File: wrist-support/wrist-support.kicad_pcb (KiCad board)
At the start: 2 copper layers, 90.5 x 59 mm, 4 parts

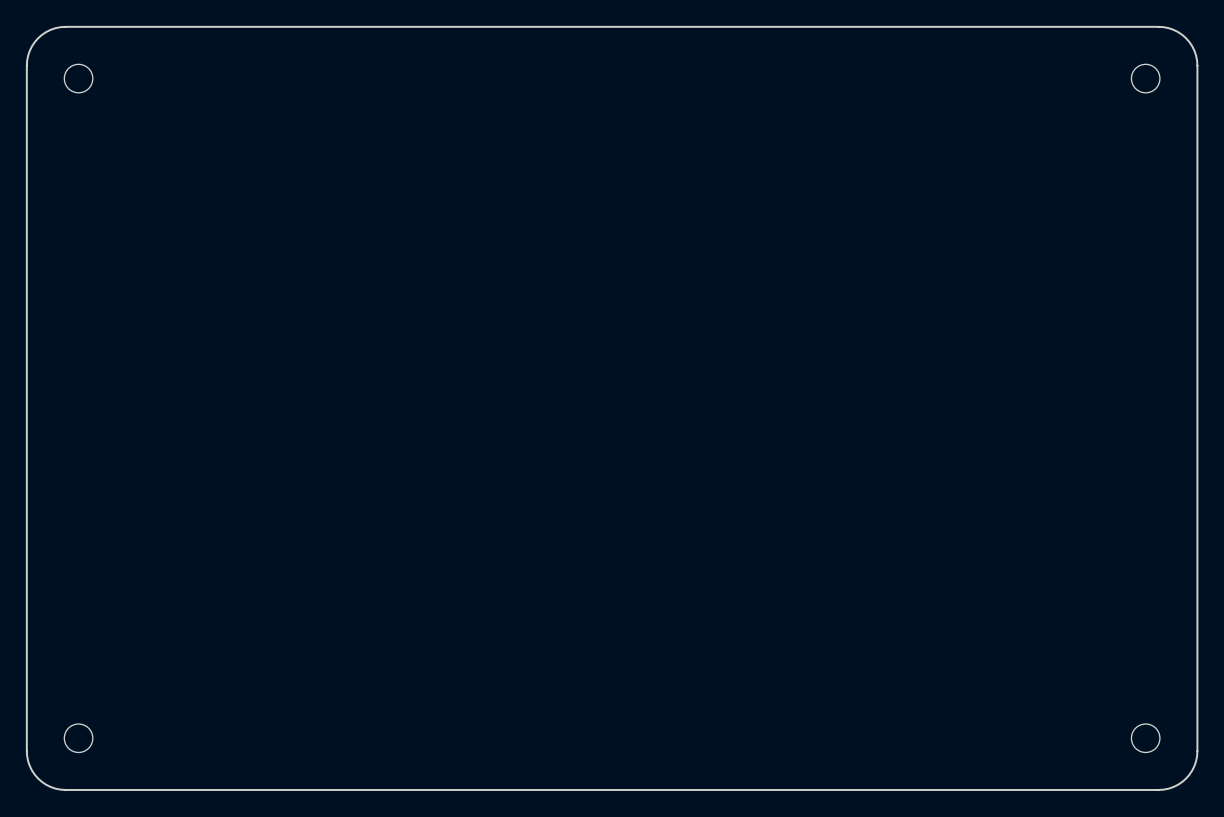
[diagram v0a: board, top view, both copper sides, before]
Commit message: Add gerbers and assembly files
M  .gitignore
M  MyFootprints.pretty/MountingHole_2.2mm_M2_ISO7380_Pad.kicad_mod
M  MySymbols.kicad_sym
M  README.md
M  drawborder.py
A  jlcpcb/gerber/optical-keyboard-mx-B_Cu.gbl
A  jlcpcb/gerber/optical-keyboard-mx-B_Mask.gbs
A  jlcpcb/gerber/optical-keyboard-mx-B_Paste.gbp
A  jlcpcb/gerber/optical-keyboard-mx-B_Silkscreen.gbo
A  jlcpcb/gerber/optical-keyboard-mx-Edge_Cuts.gm1
A  jlcpcb/gerber/optical-keyboard-mx-F_Cu.gtl
A  jlcpcb/gerber/optical-keyboard-mx-F_Mask.gts
A  jlcpcb/gerber/optical-keyboard-mx-F_Paste.gtp
A  jlcpcb/gerber/optical-keyboard-mx-F_Silkscreen.gto
A  jlcpcb/gerber/optical-keyboard-mx-NPTH-drl_map.gbr
A  jlcpcb/gerber/optical-keyboard-mx-NPTH.drl
A  jlcpcb/gerber/optical-keyboard-mx-PTH-drl_map.gbr
A  jlcpcb/gerber/optical-keyboard-mx-PTH.drl
M  led_driver.kicad_sch
M  mounting-hw.kicad_sch
M  optical-keyboard-mx.kicad_pcb
M  optical-keyboard-mx.kicad_sch
M  placefp.py
M  switch-plate/.gitignore
A  switch-plate/jlcpcb/gerber/switch-plate-B_Cu.gbl
A  switch-plate/jlcpcb/gerber/switch-plate-B_Mask.gbs
A  switch-plate/jlcpcb/gerber/switch-plate-B_Paste.gbp
A  switch-plate/jlcpcb/gerber/switch-plate-B_Silkscreen.gbo
A  switch-plate/jlcpcb/gerber/switch-plate-Edge_Cuts.gm1
A  switch-plate/jlcpcb/gerber/switch-plate-F_Cu.gtl
A  switch-plate/jlcpcb/gerber/switch-plate-F_Mask.gts
A  switch-plate/jlcpcb/gerber/switch-plate-F_Paste.gtp
A  switch-plate/jlcpcb/gerber/switch-plate-F_Silkscreen.gto
A  switch-plate/jlcpcb/gerber/switch-plate-NPTH-drl_map.gbr
A  switch-plate/jlcpcb/gerber/switch-plate-NPTH.drl
A  switch-plate/jlcpcb/gerber/switch-plate-PTH-drl_map.gbr
A  switch-plate/jlcpcb/gerber/switch-plate-PTH.drl
M  switch-plate/switch-plate.kicad_pcb
M  switch-plate/switch-plate.kicad_prl
M  switch.kicad_sch
M  wrist-support/.gitignore
A  wrist-support/jlcpcb/gerber/wrist-support-B_Cu.gbl
A  wrist-support/jlcpcb/gerber/wrist-support-B_Mask.gbs
A  wrist-support/jlcpcb/gerber/wrist-support-B_Paste.gbp
A  wrist-support/jlcpc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
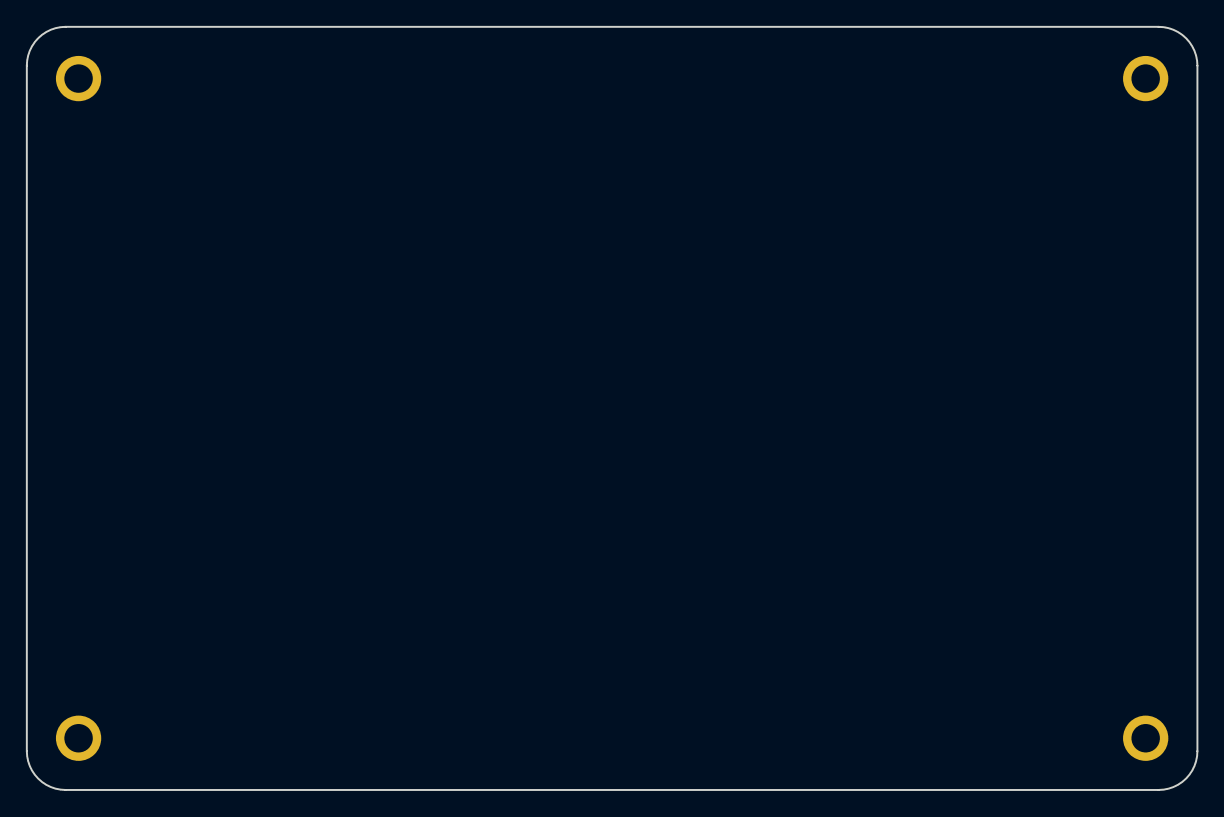
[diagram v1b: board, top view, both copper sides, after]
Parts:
- HS1, HS2, HS3, HS4: footprint MyFootprints:MountingHole_2.2mm_M2_jlcpcb -> MyFootprints:MountingHole_2.2mm_M2_ISO7380_Pad
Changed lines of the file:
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@@
       (layerselection 0x00010fc_ffffffff)
       (disableapertmacros false)
-      (usegerberextensions false)
-      (usegerberattributes true)
-      (usegerberadvancedattributes true)
-      (creategerberjobfile true)
+      (usegerberextensions true)
+      (usegerberattributes false)
+      (usegerberadvancedattributes false)
+      (creategerberjobfile false)
       (svguseinch false)
       (svgprecision 6)
@@
       (psa4output false)
       (plotreference true)
-      (plotvalue true)
+      (plotvalue false)
       (plotinvisibletext false)
       (sketchpadsonfab false)
-      (subtractmaskfromsilk false)
+      (subtractmaskfromsilk true)
       (outputformat 1)
       (mirror false)
-      (drillshape 1)
+      (drillshape 0)
       (scaleselection 1)
-      (outputdirectory "")
+      (outputdirectory "jlcpcb/gerber/")
     )
   )
   (net 0 "")
-  (footprint "MyFootprints:MountingHole_2.2mm_M2_jlcpcb" (layer "F.Cu")
+  (footprint "MyFootprints:MountingHole_2.2mm_M2_ISO7380_Pad" (layer "F.Cu")
     (at 4 55)
-    (descr "Mounting Hole 2.2mm, no annular, M2")
-    (tags "mounting hole 2.2mm no annular m2")
+    (descr "Mounting Hole 2.2mm, M2, ISO7380")
+    (tags "mounting hole 2.2mm m2 iso7380")
     (property "Sheetfile" "wrist-support.kicad_sch")
     (property "Sheetname" "")
     (attr exclude_from_pos_files)
-    (fp_text reference "HS1" (at 0 -3.2) (layer "Dwgs.User")
+    (fp_text reference "HS1" (at 0 -2.75) (layer "Dwgs.User")
       (effects (font (size 1 1) (thickness 0.15)))
     )
-    (fp_text value "MountingHoleSprt" (at 0 3.2) (layer "F.Fab")
+    (fp_text value "MountingHoleSprt" (at 0 2.75) (layer "F.Fab")
       (effects (font (size 1 1) (thickness 0.15)))
     )
@@
       (effects (font (size 1 1) (thickness 0.15)))
     )
-    (fp_circle (center 0 0) (end 2 0) (layer "Dwgs.User") (width 0.12) (fill none))
-    (fp_circle (center 0 0) (end 1.45 0) (layer "F.CrtYd") (width 0.05) (fill none))
-    (pad "" np_thru_hole circle (at 0 0) (size 2.2 2.2) (drill 2.2) (layers *.Cu *.Mask))
+    (fp_circle (center 0 0) (end 1.75 0) (layer "Cmts.User") (width 0.15) (fill none))
+    (fp_circle (center 0 0) (end 2 0) (layer "F.CrtYd") (width 0.05) (fill none))
+    (pad "" thru_hole circle (at 0 0) (size 3.5 3.5) (drill 2.2) (layers *.Cu *.Mask))
   )
-  (footprint "MyFootprints:MountingHole_2.2mm_M2_jlcpcb" (layer "F.Cu")
+  (footprint "MyFootprints:MountingHole_2.2mm_M2_ISO7380_Pad" (layer "F.Cu")
     (at 86.5 55)
-    (descr "Mounting Hole 2.2mm, no annular, M2")
-    (tags "mounting hole 2.2mm no annular m2")
+    (descr "Mounting Hole 2.2mm, M2, ISO7380")
+    (tags "mounting hole 2.2mm m2 iso7380")
     (property "Sheetfile" "wrist-support.kicad_sch")
     (property "Sheetname" "")
     (attr exclude_from_pos_files)
-    (fp_text reference "HS2" (at 0 -3.2) (layer "Dwgs.User")
+    (fp_text reference "HS2" (at 0 -2.75) (layer "Dwgs.User")
       (effects (font (size 1 1) (thickness 0.15)))
     )
-    (fp_text value "MountingHoleSprt" (at 0 3.2) (layer "F.Fab")
+    (fp_text value "MountingHoleSprt" (at 0 2.75) (layer "F.Fab")
       (effects (font (size 1 1) (thickness 0.15)))
     )
@@
       (effects (font (size 1 1) (thickness 0.15)))
     )
-    (fp_circle (center 0 0) (end 2 0) (layer "Dwgs.User") (width 0.12) (fill none))
-    (fp_circle (center 0 0) (end 1.45 0) (layer "F.CrtYd") (width 0.05) (fill none))
-    (pad "" np_thru_hole circle (at 0 0) (size 2.2 2.2) (drill 2.2) (layers *.Cu *.Mask))
+    (fp_circle (center 0 0) (end 1.75 0) (layer "Cmts.User") (width 0.15) (fill none))
+    (fp_circle (center 0 0) (end 2 0) (layer "F.CrtYd") (width 0.05) (fill none))
+    (pad "" thru_hole circle (at 0 0) (size 3.5 3.5) (drill 2.2) (layers *.Cu *.Mask))
   )
-  (footprint "MyFootprints:MountingHole_2.2mm_M2_jlcpcb" (layer "F.Cu")
+  (footprint "MyFootprints:MountingHole_2.2mm_M2_ISO7380_Pad" (layer "F.Cu")
     (at 4 4)
-    (descr "Mounting Hole 2.2mm, no annular, M2")
-    (tags "mounting hole 2.2mm no annular m2")
+    (descr "Mounting Hole 2.2mm, M2, ISO7380")
+    (tags "mounting hole 2.2mm m2 iso7380")
     (property "Sheetfile" "wrist-support.kicad_sch")
     (property "Sheetname" "")
     (attr exclude_from_pos_files)
-    (fp_text reference "HS3" (at 0 -3.2) (layer "Dwgs.User")
+    (fp_text reference "HS3" (at 0 -2.75) (layer "Dwgs.User")
       (effects (font (size 1 1) (thickness 0.15)))
     )
-    (fp_text value "MountingHoleSprt" (at 0 3.2) (layer "F.Fab")
+    (fp_text value "MountingHoleSprt" (at 0 2.75) (layer "F.Fab")
       (effects (font (size 1 1) (thickness 0.15)))
     )
@@
       (effects (font (size 1 1) (thickness 0.15)))
     )
-    (fp_circle (center 0 0) (end 2 0) (layer "Dwgs.User") (width 0.12) (fill none))
-    (fp_circle (center 0 0) (end 1.45 0) (layer "F.CrtYd") (width 0.05) (fill none))
-    (pad "" np_thru_hole circle (at 0 0) (size 2.2 2.2) (drill 2.2) (layers *.Cu *.Mask))
+    (fp_circle (center 0 0) (end 1.75 0) (layer "Cmts.User") (width 0.15) (fill none))
+    (fp_circle (center 0 0) (end 2 0) (layer "F.CrtYd") (width 0.05) (fill none))
+    (pad "" thru_hole circle (at 0 0) (size 3.5 3.5) (drill 2.2) (layers *.Cu *.Mask))
   )
-  (footprint "MyFootprints:MountingHole_2.2mm_M2_jlcpcb" (layer "F.Cu")
+  (footprint "MyFootprints:MountingHole_2.2mm_M2_ISO7380_Pad" (layer "F.Cu")
     (at 86.5 4)
-    (descr "Mounting Hole 2.2mm, no annular, M2")
-    (tags "mounting hole 2.2mm no annular m2")
+    (descr "Mounting Hole 2.2mm, M2, ISO7380")
+    (tags "mounting hole 2.2mm m2 iso7380")
     (property "Sheetfile" "wrist-support.kicad_sch")
     (property "Sheetname" "")
     (attr exclude_from_pos_files)
-    (fp_text reference "HS4" (at 0 -3.2) (layer "Dwgs.User")
+    (fp_text reference "HS4" (at 0 -2.75) (layer "Dwgs.User")
       (effects (font (size 1 1) (thickness 0.15)))
     )
-    (fp_text value "MountingHoleSprt" (at 0 3.2) (layer "F.Fab")
+    (fp_text value "MountingHoleSprt" (at 0 2.75) (layer "F.Fab")
       (effects (font (size 1 1) (thickness 0.15)))
     )
@@
       (effects (font (size 1 1) (thickness 0.15)))
     )
-    (fp_circle (center 0 0) (end 2 0) (layer "Dwgs.User") (width 0.12) (fill none))
-    (fp_circle (center 0 0) (end 1.45 0) (layer "F.CrtYd") (width 0.05) (fill none))
-    (pad "" np_thru_hole circle (at 0 0) (size 2.2 2.2) (drill 2.2) (layers *.Cu *.Mask))
+    (fp_circle (center 0 0) (end 1.75 0) (layer "Cmts.User") (width 0.15) (fill none))
+    (fp_circle (center 0 0) (end 2 0) (layer "F.CrtYd") (width 0.05) (fill none))
+    (pad "" thru_hole circle (at 0 0) (size 3.5 3.5) (drill 2.2) (layers *.Cu *.Mask))
   )
   (gr_arc (start 87.5 0) (mid 89.62132 0.87868) (end 90.5 3) (layer "Edge.Cuts") (width 0.15))
